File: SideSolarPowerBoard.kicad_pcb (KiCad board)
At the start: 2 copper layers, 46 x 53.6 mm, 22 parts, among them U1 SPV1040

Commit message: Migrate project to KiCad 7
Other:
- net class Default removed
- net class Power removed
- net class pogo-pin removed

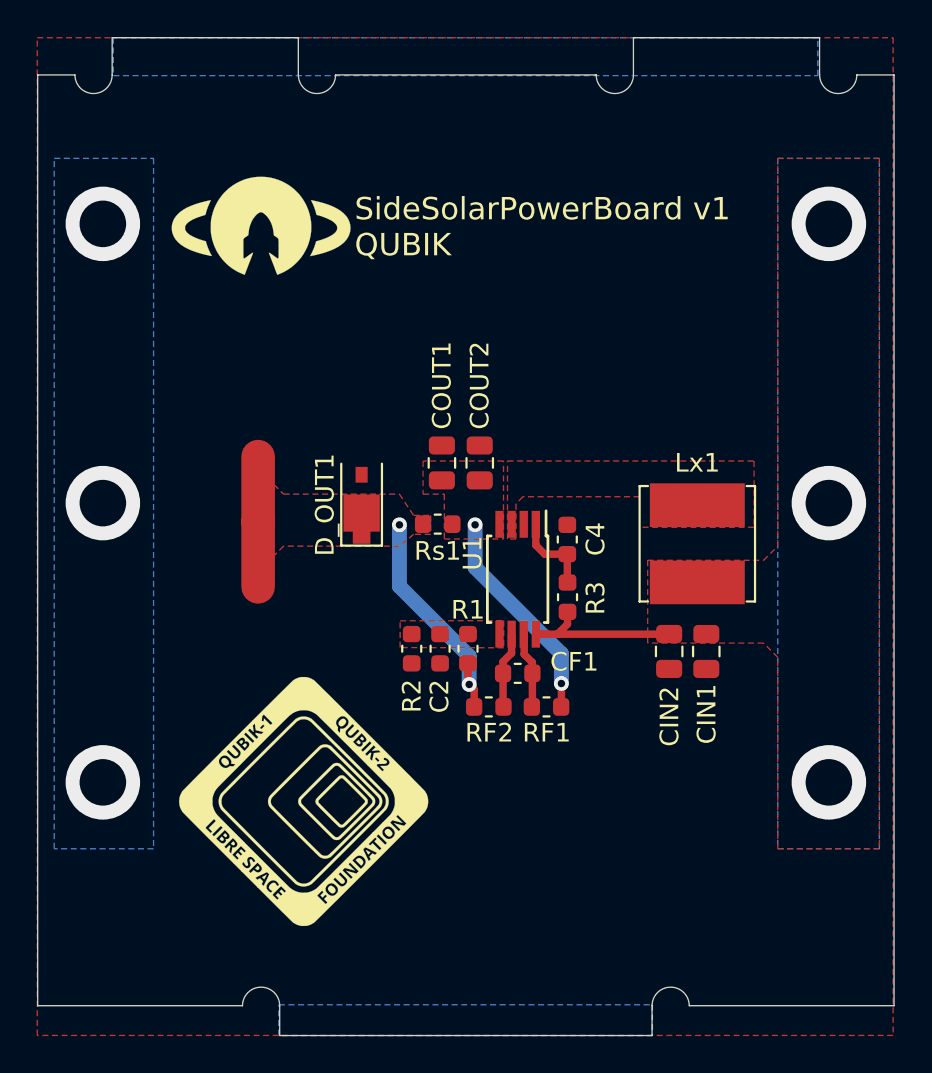
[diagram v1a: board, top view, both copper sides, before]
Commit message: Quickly add a sensor and a connector
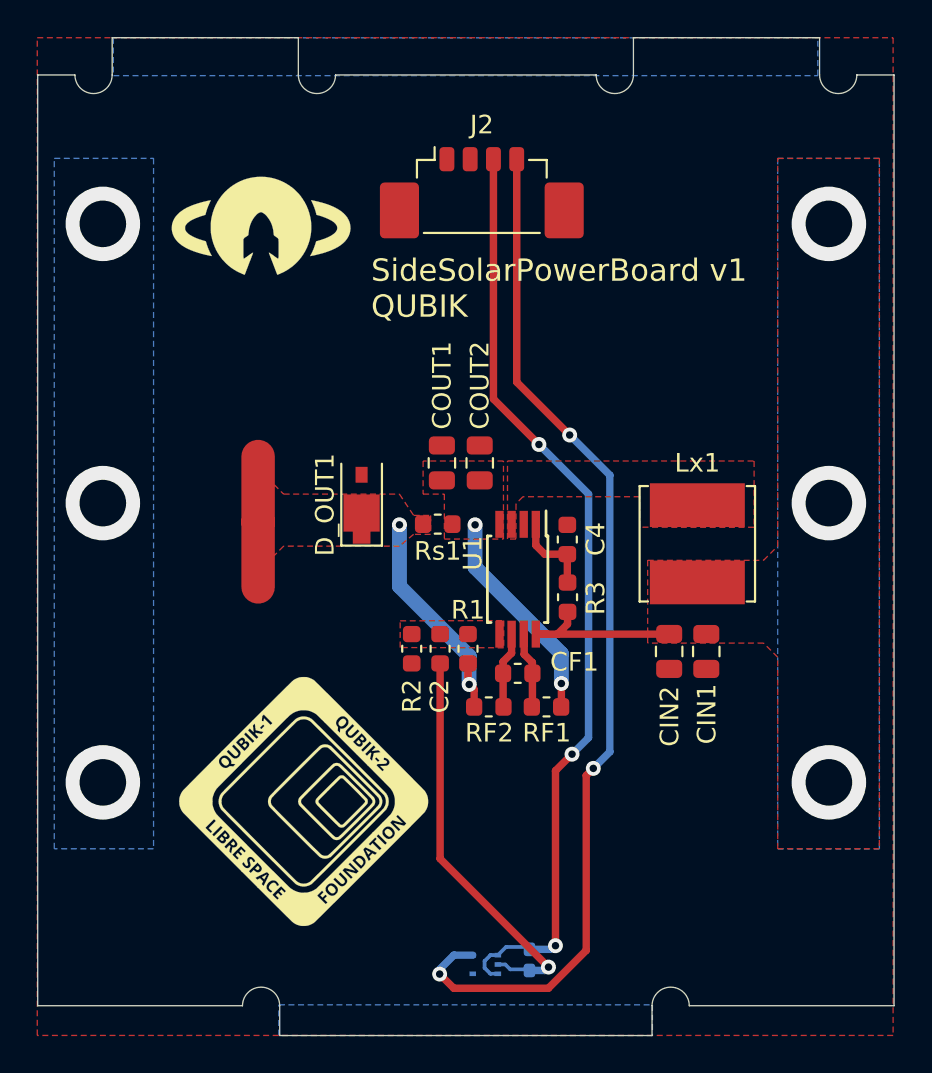
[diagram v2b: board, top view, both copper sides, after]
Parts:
- added C1: C, Capacitor_SMD:C_0402_1005Metric_Pad0.74x0.62mm_HandSolder, B.Cu at (151.9, 121.0)
- added J2: Conn_01x04, Connector_Molex:Molex_PicoBlade_53398-0471_1x04-1MP_P1.25mm_Vertical, F.Cu at (149.4, 79.3)
- added U2: ~, POQUITO_Panel_Library:WSOF-5, B.Cu at (149.5, 121.3)
- moved REF** 5.65 mm to (142.9, 122.2)
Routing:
- net /LIGHT_OUT: track 0.00 -> 56.4 mm, vias 0 -> 3
- net /LIGHT_VDD: track 0.00 -> 50.5 mm, vias 0 -> 3
- net GND: track 0.00 -> 21.7 mm, vias 3 -> 4

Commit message: Move new kicad_pcb file
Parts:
- moved RF2 7.70 mm to (149.6, 115.1)
- moved RF1 7.70 mm to (153.0, 115.1)
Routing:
- net /VOUT: track 11.7 -> 17343.1 mm, vias 2 -> 5
- net /ICTRL-: track 4.04 -> 12.0 mm
- net /ICTRL+: track 4.00 -> 11.8 mm
- net /VBAT+: track 19.6 -> 27.2 mm
- net /LIGHT_OUT: track 56.4 -> 59.5 mm
- net /LIGHT_VDD: track 50.5 -> 51.8 mm
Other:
- copper layers 2 -> 6

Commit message: Add all missing connections
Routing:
- net /MTQ_2: track 0.00 -> 17340.8 mm, vias 0 -> 4
- net /VOUT: track 17343.1 -> 19.5 mm, vias 5 -> 2
- net /MTQ_1: track 0.00 -> 15.1 mm
- net /VBAT+: track 27.2 -> 34.8 mm
- net /LIGHT_OUT: track 59.5 -> 60.2 mm

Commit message: Add logos
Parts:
- removed the REF** at (137.5, 81.6)
- removed the REF** at (142.9, 122.2)
- added G***: LOGO, POQUITO_Panel_Library:unilu_snt_logo, F.Cu at (135.8, 84.6)
- added G***: LOGO, POQUITO_Panel_Library:POQUITO_logo, B.Cu at (142.8, 121.6)
- added REF**: OSHW-Logo_11.4x12mm_SilkScreen, Symbol:OSHW-Logo_11.4x12mm_SilkScreen, F.Cu at (161.2, 116.1)
- added kibuzzard-64FE2F42: G***, kibuzzard-64FE2F42, F.Cu at (132.5, 101.3)
- added kibuzzard-64FE2F6D: G***, kibuzzard-64FE2F6D, F.Cu at (140.2, 101.3)
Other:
- board text added: "Originally designed by the Libre Space Foundation"
- board text added: "SideSolarPowerBoard v2 POQUITO"
- board text removed: "SideSolarPowerBoard v1 QUBIK"

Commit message: Fix connection of MTQ2 to not overlap run
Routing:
- net /MTQ_1: track 15.1 -> 16.3 mm, vias 0 -> 1
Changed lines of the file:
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@@
   (segment (start 149.818 120.782) (end 150.218 120.782) (width 0.2) (layer "B.Cu") (net 10))
   (segment (start 155.091 112.2984) (end 156.5896 113.797) (width 0.4) (layer "B.Cu") (net 10))
-  (segment (start 134.981 78.027) (end 133.12 79.888) (width 0.4) (layer "F.Cu") (net 11))
-  (segment (start 147.481 78.027) (end 134.981 78.027) (width 0.4) (layer "F.Cu") (net 11))
+  (segment (start 132 76.1) (end 133.927 78.027) (width 0.4) (layer "F.Cu") (net 11))
+  (segment (start 133.927 78.027) (end 147.481 78.027) (width 0.4) (layer "F.Cu") (net 11))
+  (via (at 132 76.1) (size 0.8) (drill 0.4) (layers "F.Cu" "B.Cu") (net 11))
   (segment (start 147.852 76.078) (end 133.628 76.078) (width 0.4) (layer "F.Cu") (net 12))
   (segment (start 148.731 76.957) (end 147.852 76.078) (width 0.4) (layer "F.Cu") (net 12))

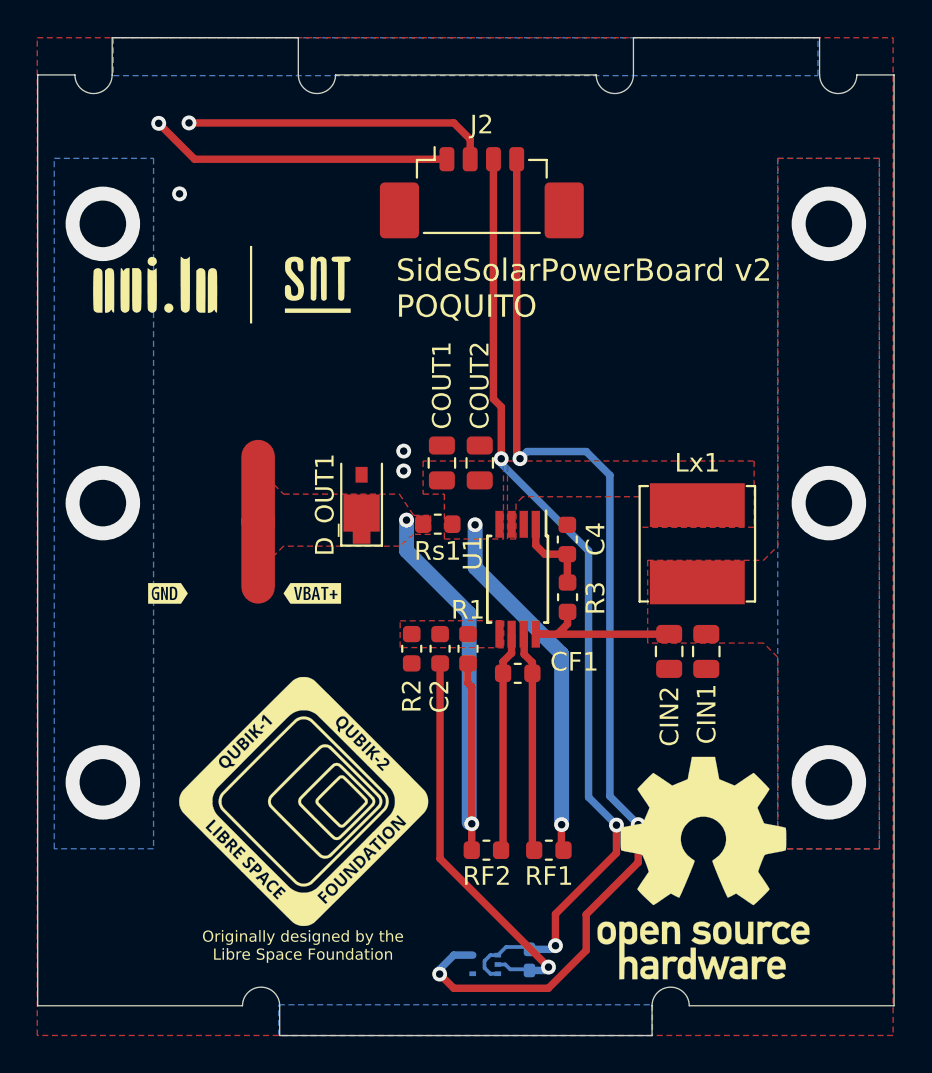
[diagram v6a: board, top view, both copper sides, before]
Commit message: Update to pogo pin ADCS design
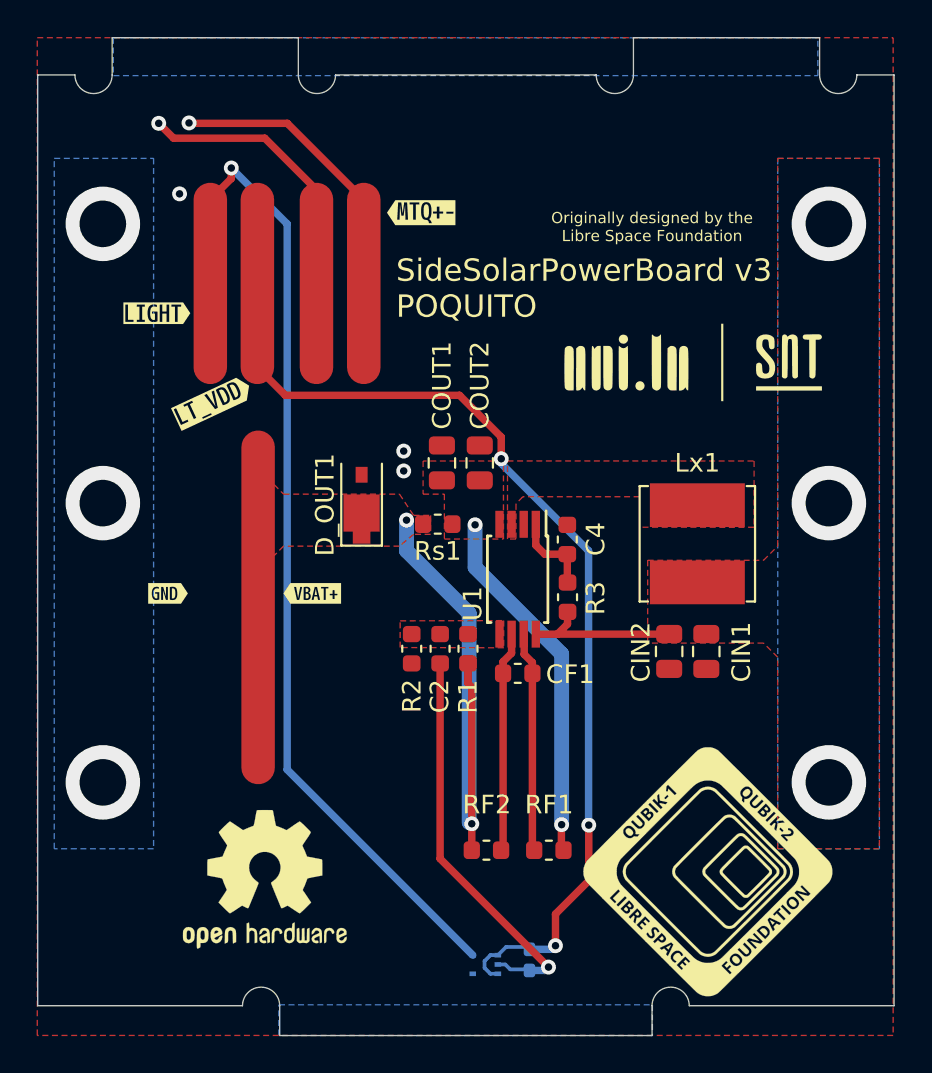
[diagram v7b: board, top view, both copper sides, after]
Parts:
- removed J2: Conn_01x04, Connector_Molex:Molex_PicoBlade_53398-0471_1x04-1MP_P1.25mm_Vertical
- removed the REF** at (161.2, 116.1)
- added REF**: OSHW-Logo2_9.8x8mm_SilkScreen, Symbol:OSHW-Logo2_9.8x8mm_SilkScreen, F.Cu at (137.7, 116.7)
- added kibuzzard-658D6171: G***, kibuzzard-658D6171, F.Cu at (131.9, 86.3)
- added kibuzzard-658D6185: G***, kibuzzard-658D6185, F.Cu at (134.9, 91.1)
- added kibuzzard-658D61DC: G***, kibuzzard-658D61DC, F.Cu at (146.1, 80.9)
- moved G*** 25.7 mm to (161.1, 88.8)
- moved REF** 22.0 mm to (161.5, 116.3)
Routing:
- net /MTQ_2: track 17340.8 -> 17363.9 mm, vias 4 -> 5
- net /MTQ_1: track 16.3 -> 0.00 mm, vias 1 -> 0
- net /VBAT+: track 34.8 -> 45.0 mm
- net /LIGHT_VDD: track 51.8 -> 59.1 mm
- net /LIGHT_OUT: track 60.2 -> 58.8 mm, vias 3 -> 1
- net /PV+: track 9.23 -> 8.60 mm
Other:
- board text added: "SideSolarPowerBoard v3 POQUITO"
- board text removed: "SideSolarPowerBoard v2 POQUITO"

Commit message: Fix position of Lx
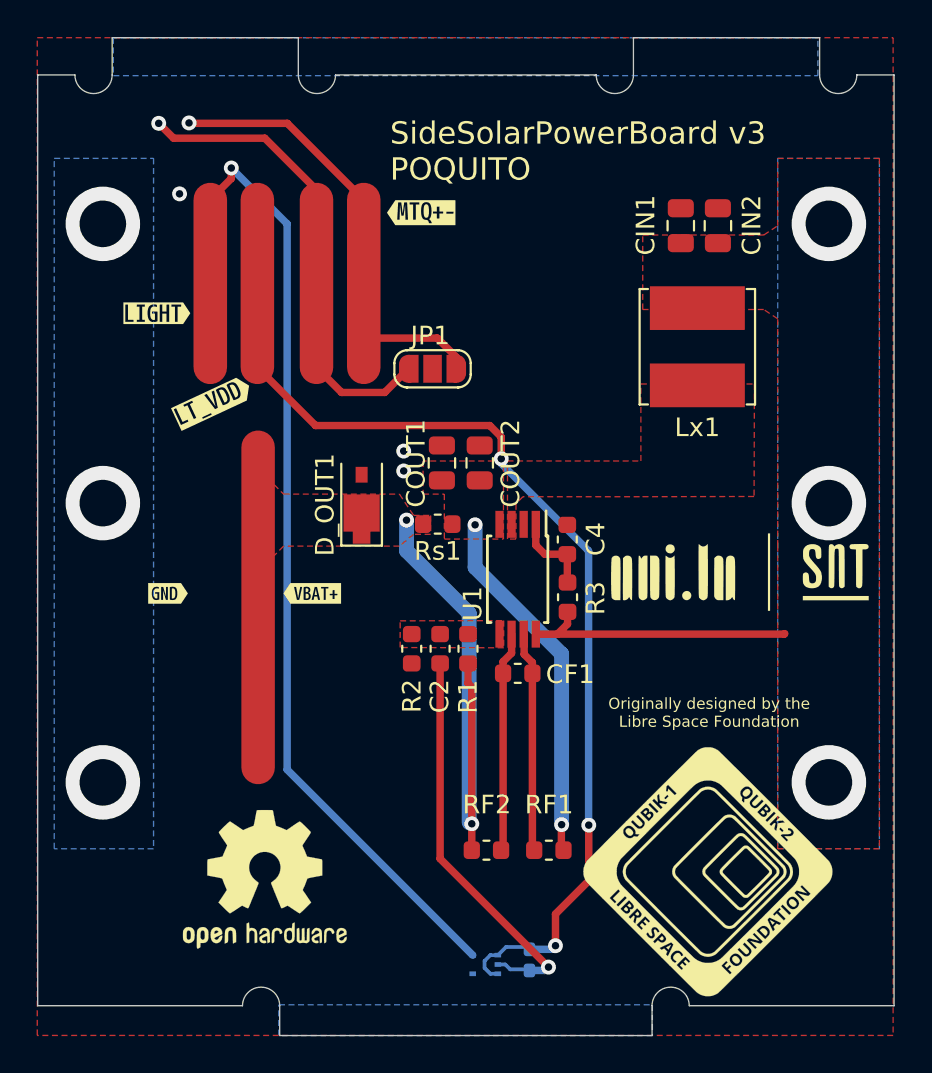
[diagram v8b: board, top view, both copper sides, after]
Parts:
- added JP1: SolderJumper_3_Open, Jumper:SolderJumper-3_P1.3mm_Open_RoundedPad1.0x1.5mm_NumberLabels, F.Cu at (146.7, 89.3)
- C1: value C -> 100nF
- U2: value ~ -> BH1682FVC
- moved CIN2 23.0 mm to (162.0, 81.6), turned to 90 degrees
- moved CIN1 22.9 mm to (160.0, 81.6), turned to 90 degrees
- moved G*** 11.5 mm to (163.6, 100.0)
- moved Lx1 10.6 mm to (160.9, 88.1), turned to -90 degrees
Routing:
- net /MTQ_2: track 17363.9 -> 17376.0 mm
- net /PV+: track 8.60 -> 14.8 mm
